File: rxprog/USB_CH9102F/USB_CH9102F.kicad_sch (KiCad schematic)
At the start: 20 parts, among them J1 5077CR-16-SMC2-BK-TR, J2 USB-C OPT, J3 Serial In/Out Full, J4 GPIO, J5 SUSPEND, J6 /SUSPEND, J7 /ACT, J8 /RST, J9 Serial In/Out, SW1 3P-SW, U1 CH9102F, U2 NJU7223DL1-33

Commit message: Update: add USB/Register, LED
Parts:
- removed J2: USB-C OPT, Connector_PinHeader_2.54mm:PinHeader_1x04_P2.54mm_Vertical, symbol Connector_Generic:Conn_01x04
- added D2, D3: RED, LED_SMD:LED_0603_1608Metric_Pad1.05x0.95mm_HandSolder, symbol LED:IRL81A
- added J2: USB/OPT, Connector_PinHeader_2.54mm:PinHeader_1x02_P2.54mm_Vertical, symbol Connector_Generic:Conn_01x02
- added R2, R3: 10K, Resistor_SMD:R_0603_1608Metric_Pad0.98x0.95mm_HandSolder, symbol akizuki:R
- added R4, R5: 2K, Resistor_SMD:R_0603_1608Metric_Pad0.98x0.95mm_HandSolder, symbol akizuki:R
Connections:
- net GND: now also R2.2, R3.2
- net at J1.A5 (CC1): now also R2.1
- net at J1.B5 (CC2): now also R3.1
- net at J1.A8 (SBU1): now also J2.1 (Pin_1)
- net at J1.B8 (SBU2): now also J2.2 (Pin_2)
- net at J4.1 (Pin_1), U1.14 (TXS/GPIO0): now also R4.1
- net at J4.2 (Pin_2), U1.13 (RXS/GPIO1): now also R5.1
- net at C2.2, J3.4 (Pin_4), J4.6 (Pin_6)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: now also D2.2 (A), D3.2 (A)
- new net: D3.1 (K), R5.2
- new net: D2.1 (K), R4.2
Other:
- note removed: "CC1"
- note removed: "CC2"
- moved on the sheet: J5, J6, J7, J8

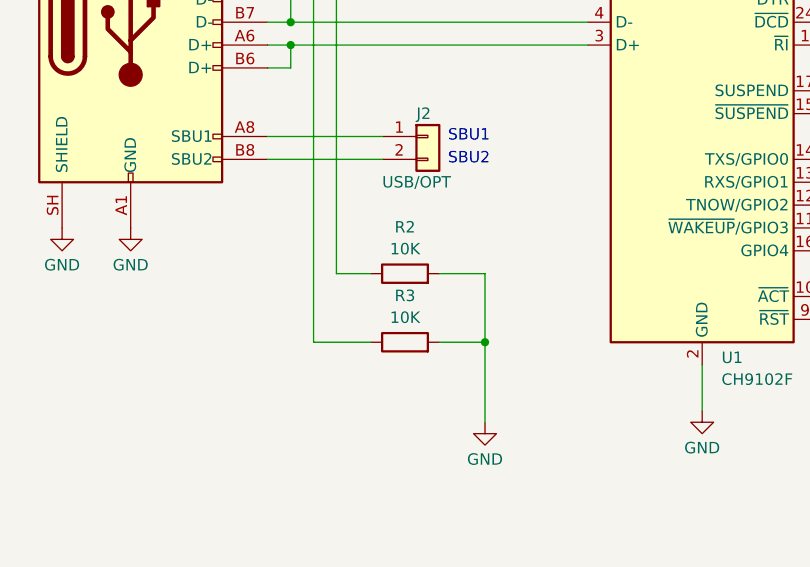
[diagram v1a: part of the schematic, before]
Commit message: Update: CC1 pull down register
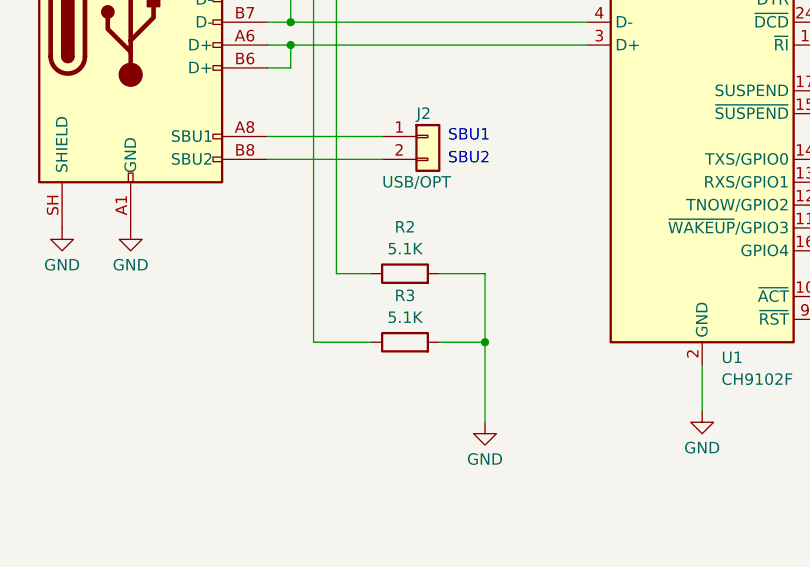
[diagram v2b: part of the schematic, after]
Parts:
- R2, R3: value 10K -> 5.1K
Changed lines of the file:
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@@
 			)
 		)
-		(property "Value" "10K"
+		(property "Value" "5.1K"
 			(at 80.01 140.7738 0)
 			(show_name no)
@@
 			)
 		)
-		(property "Value" "10K"
+		(property "Value" "5.1K"
 			(at 80.01 133.1538 0)
 			(show_name no)
